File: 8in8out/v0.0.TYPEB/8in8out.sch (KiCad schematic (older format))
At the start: 60 parts, among them IC1 ATTINY48-A, J1 RJ45, J2 RJ45, J3 CONN_6, K110 G5T-1-12VDC, K120 G5T-1-12VDC, K130 G5T-1-12VDC, K140 G5T-1-12VDC, K150 G5T-1-12VDC, K160 G5T-1-12VDC, K170 G5T-1-12VDC, K180 G5T-1-12VDC, P1 CONN_5, P100 CONN_2, P101 CONN_2, P102 CONN_2, P103 CONN_2, P105 CONN_2, P106 CONN_2, P110 CONN_2, P120 CONN_2, P130 CONN_2, P140 CONN_2, P150 CONN_2, P160 CONN_2, P170 CONN_2, P180 CONN_2, P2 CONN_5, P3 CONN_10X2, P4 CONN_2, U1 7805, U10 OPTO-TRANSISTOR, U2 ULN2803, U20 OPTO-TRANSISTOR, U30 OPTO-TRANSISTOR, U40 OPTO-TRANSISTOR, U50 OPTO-TRANSISTOR, U60 OPTO-TRANSISTOR, U70 OPTO-TRANSISTOR, U80 OPTO-TRANSISTOR

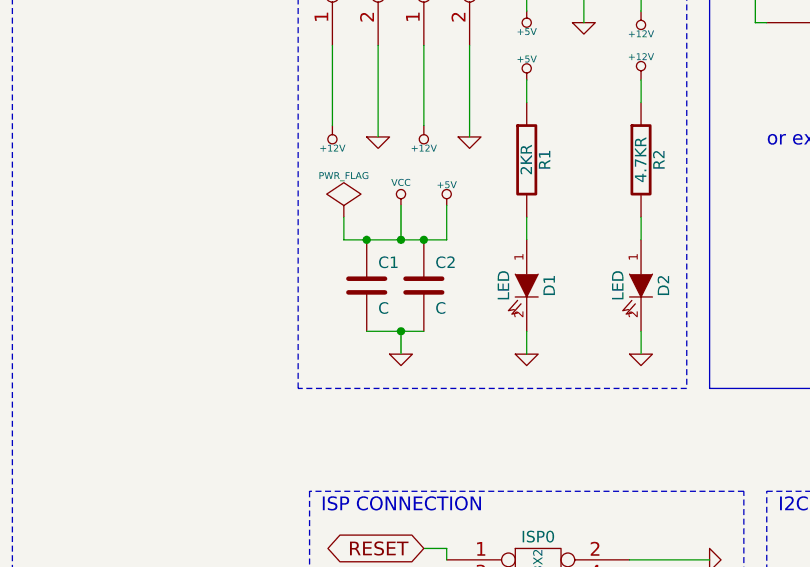
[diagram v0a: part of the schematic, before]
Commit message: ajout capa C3
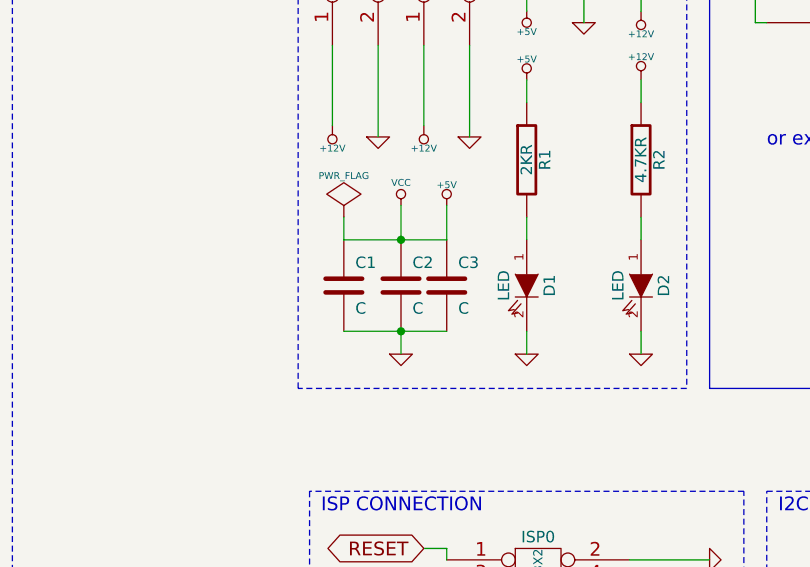
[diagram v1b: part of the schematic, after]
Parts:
- added C3: C, symbol C
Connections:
- net +5V: now also C3.1
- net GND: now also C3.2
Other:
- moved on the sheet: C1, C2
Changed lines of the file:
@@
-EESchema Schematic File Version 2  date sam. 01 juin 2013 17:55:48 CEST
+EESchema Schematic File Version 2  date dim. 02 juin 2013 15:29:56 CEST
 LIBS:g5la-1-12vdc
 LIBS:power
@@
 Sheet 1 1
 Title "8in 8relays I2C board"
-Date "1 jun 2013"
+Date "2 jun 2013"
 Rev "V0.2"
 Comp "XPLDUINO project"
@@
 L C C1
 U 1 1 5067601F
-P 10550 3650
-F 0 "C1" H 10600 3750 50  0000 L CNN
-F 1 "C" H 10600 3550 50  0000 L CNN
-F 2 "" H 10550 3650 60  0001 C CNN
-F 3 "" H 10550 3650 60  0001 C CNN
-	1    10550 3650
+P 10450 3650
+F 0 "C1" H 10500 3750 50  0000 L CNN
+F 1 "C" H 10500 3550 50  0000 L CNN
+F 2 "" H 10450 3650 60  0001 C CNN
+F 3 "" H 10450 3650 60  0001 C CNN
+	1    10450 3650
 	1    0    0    -1
 $EndComp
@@
 L C C2
 U 1 1 5067602E
-P 10800 3650
-F 0 "C2" H 10850 3750 50  0000 L CNN
-F 1 "C" H 10850 3550 50  0000 L CNN
-F 2 "" H 10800 3650 60  0001 C CNN
-F 3 "" H 10800 3650 60  0001 C CNN
-	1    10800 3650
+P 10700 3650
+F 0 "C2" H 10750 3750 50  0000 L CNN
+F 1 "C" H 10750 3550 50  0000 L CNN
+F 2 "" H 10700 3650 60  0001 C CNN
+F 3 "" H 10700 3650 60  0001 C CNN
+	1    10700 3650
 	1    0    0    -1
 $EndComp
@@
 	10450 3350 10450 3450
 Wire Wire Line
-	10450 3450 10900 3450
-Connection ~ 10550 3450
-Wire Wire Line
 	10900 3450 10900 3300
-Connection ~ 10800 3450
 Wire Wire Line
 	10700 3300 10700 3450
-Connection ~ 10700 3450
-Wire Wire Line
-	10550 3850 10800 3850
+Wire Wire Line
+	10450 3850 10900 3850
 Wire Wire Line
 	10700 3850 10700 3950
@@
 	1    0    0    -1
 $EndComp
+$Comp
+L C C3
+U 1 1 51AB4C03
+P 10900 3650
+F 0 "C3" H 10950 3750 50  0000 L CNN
+F 1 "C" H 10950 3550 50  0000 L CNN
+F 2 "" H 10900 3650 60  0001 C CNN
+F 3 "" H 10900 3650 60  0001 C CNN
+	1    10900 3650
+	1    0    0    -1
+$EndComp
+Connection ~ 10700 3450
+Wire Wire Line
+	10450 3450 10900 3450
 $EndSCHEMATC

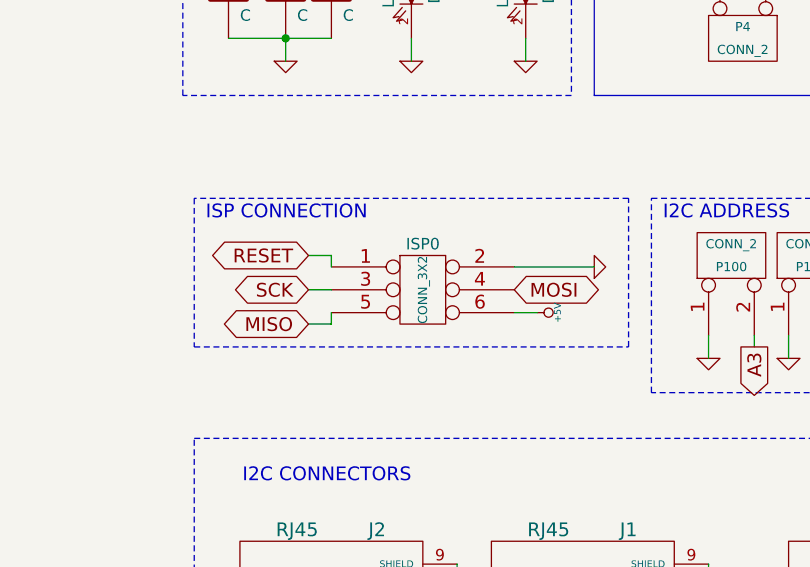
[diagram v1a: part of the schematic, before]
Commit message: correction connecteur ISP
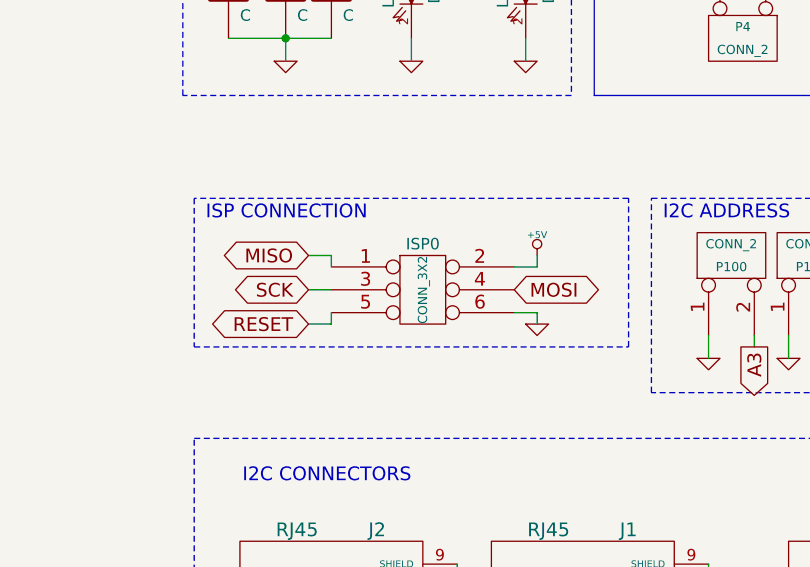
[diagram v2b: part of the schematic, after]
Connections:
- net +5V: now also ISP0.2; no longer ISP0.6
- net GND: now also ISP0.6; no longer ISP0.2
- net MISO: now also ISP0.1; no longer ISP0.5
- net RESET: now also ISP0.5; no longer ISP0.1
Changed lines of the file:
@@
-EESchema Schematic File Version 2  date dim. 02 juin 2013 15:29:56 CEST
+EESchema Schematic File Version 2
 LIBS:g5la-1-12vdc
 LIBS:power
@@
 L +5V #PWR03
 U 1 1 50670686
-P 11800 5050
-F 0 "#PWR03" H 11800 5140 20  0001 C CNN
-F 1 "+5V" H 11800 5140 30  0000 C CNN
-F 2 "" H 11800 5050 60  0001 C CNN
-F 3 "" H 11800 5050 60  0001 C CNN
-	1    11800 5050
-	0    1    1    0
+P 11800 4800
+F 0 "#PWR03" H 11800 4890 20  0001 C CNN
+F 1 "+5V" H 11800 4890 30  0000 C CNN
+F 2 "" H 11800 4800 60  0001 C CNN
+F 3 "" H 11800 4800 60  0001 C CNN
+	1    11800 4800
+	1    0    0    -1
 $EndComp
 Text Notes 10350 4650 0    60   ~ 0
@@
 L GND #PWR025
 U 1 1 5135D759
-P 12050 4850
-F 0 "#PWR025" H 12050 4850 30  0001 C CNN
-F 1 "GND" H 12050 4780 30  0001 C CNN
-F 2 "" H 12050 4850 60  0001 C CNN
-F 3 "" H 12050 4850 60  0001 C CNN
-	1    12050 4850
-	0    -1   -1   0
+P 11800 5100
+F 0 "#PWR025" H 11800 5100 30  0001 C CNN
+F 1 "GND" H 11800 5030 30  0001 C CNN
+F 2 "" H 11800 5100 60  0001 C CNN
+F 3 "" H 11800 5100 60  0001 C CNN
+	1    11800 5100
+	1    0    0    -1
 $EndComp
 $Comp
@@
 RESET
 Connection ~ 13700 10550
-Text GLabel 10800 4800 0    60   BiDi ~ 0
+Text GLabel 10800 5100 0    60   BiDi ~ 0
 RESET
 Text GLabel 10800 4950 0    60   BiDi ~ 0
 SCK
-Text GLabel 10800 5100 0    60   BiDi ~ 0
+Text GLabel 10800 4800 0    60   BiDi ~ 0
 MISO
 Text GLabel 11700 4950 2    60   BiDi ~ 0
@@
 Wire Wire Line
 	10900 5100 10900 5050
-Wire Wire Line
-	11700 4850 12050 4850
 $Comp
 L CONN_5 P1
@@
 Wire Wire Line
 	10450 3450 10900 3450
+Wire Wire Line
+	11700 4850 11800 4850
+Wire Wire Line
+	11800 4850 11800 4800
+Wire Wire Line
+	11800 5050 11800 5100
 $EndSCHEMATC
